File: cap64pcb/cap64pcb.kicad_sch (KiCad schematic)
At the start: 31 parts, among them J1 SM05B_SURS_TF, Q1 BSS138, Q2 BSS138, U1 MPR121QR2, U2 SPX3819M5-L-3-3

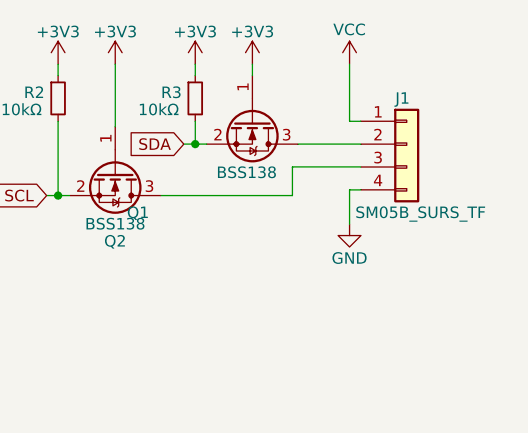
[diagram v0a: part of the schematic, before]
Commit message: reorder conn pinout
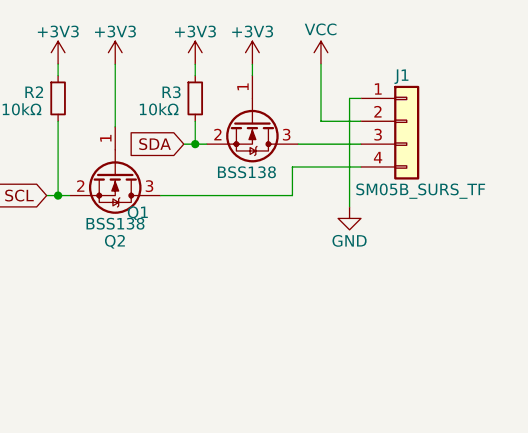
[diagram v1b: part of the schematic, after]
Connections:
- net GND: now also J1.1 (Pin_1); no longer J1.4 (Pin_4)
- net VCC: now also J1.2 (Pin_2); no longer J1.1 (Pin_1)
- net at Q1.3 (D): now also J1.3 (Pin_3); no longer J1.2 (Pin_2)
- net at Q2.3 (D): now also J1.4 (Pin_4); no longer J1.3 (Pin_3)
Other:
- moved on the sheet: J1
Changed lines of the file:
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@@
     (stroke (width 0) (type default) (color 0 0 0 0))
   )
-  (wire (pts (xy 179.07 40.005) (xy 179.07 46.355))
+  (wire (pts (xy 175.895 40.005) (xy 175.895 46.355))
     (stroke (width 0) (type default) (color 0 0 0 0))
   )
@@
     (stroke (width 0) (type default) (color 0 0 0 0))
   )
-  (wire (pts (xy 179.07 53.975) (xy 180.34 53.975))
-    (stroke (width 0) (type default) (color 0 0 0 0))
-  )
   (wire (pts (xy 58.42 50.165) (xy 58.42 52.705))
     (stroke (width 0) (type default) (color 0 0 0 0))
@@
     (stroke (width 0) (type default) (color 0 0 0 0))
   )
-  (wire (pts (xy 179.07 46.355) (xy 180.34 46.355))
+  (wire (pts (xy 175.895 46.355) (xy 180.34 46.355))
     (stroke (width 0) (type default) (color 0 0 0 0))
   )
@@
     (stroke (width 0) (type default) (color 0 0 0 0))
   )
+  (wire (pts (xy 179.07 43.815) (xy 179.07 55.88))
+    (stroke (width 0) (type default) (color 0 0 0 0))
+  )
   (wire (pts (xy 97.79 56.515) (xy 100.33 56.515))
     (stroke (width 0) (type default) (color 0 0 0 0))
@@
     (stroke (width 0) (type default) (color 0 0 0 0))
   )
+  (wire (pts (xy 180.34 43.815) (xy 179.07 43.815))
+    (stroke (width 0) (type default) (color 0 0 0 0))
+  )
   (wire (pts (xy 88.265 61.595) (xy 88.265 64.135))
     (stroke (width 0) (type default) (color 0 0 0 0))
@@
   )
   (wire (pts (xy 125.73 56.515) (xy 127 56.515))
-    (stroke (width 0) (type default) (color 0 0 0 0))
-  )
-  (wire (pts (xy 179.07 53.975) (xy 179.07 57.785))
     (stroke (width 0) (type default) (color 0 0 0 0))
   )
@@
     (pin "1")
   )
-  (symbol (lib_id "Connector_Generic:Conn_01x04") (at 185.42 48.895 0) (unit 1)
-    (in_bom yes) (on_board yes)
-    (property "Reference" "J1" (id 0) (at 184.15 43.815 0)
-      (effects (font (size 1.27 1.27)) (justify left))
-    )
-    (property "Value" "SM05B_SURS_TF" (id 1) (at 179.705 56.515 0)
-      (effects (font (size 1.27 1.27)) (justify left))
-    )
-    (property "Footprint" "Connector_JST:JST_SUR_SM04B-SURS-TF_1x04-1MP_P0.80mm_Horizontal" (id 2) (at 185.42 48.895 0)
-      (effects (font (size 1.27 1.27)) hide)
-    )
-    (property "Datasheet" "~" (id 3) (at 185.42 48.895 0)
+  (symbol (lib_id "Connector_Generic:Conn_01x04") (at 185.42 46.355 0) (unit 1)
+    (in_bom yes) (on_board yes)
+    (property "Reference" "J1" (id 0) (at 184.15 41.275 0)
+      (effects (font (size 1.27 1.27)) (justify left))
+    )
+    (property "Value" "SM05B_SURS_TF" (id 1) (at 179.705 53.975 0)
+      (effects (font (size 1.27 1.27)) (justify left))
+    )
+    (property "Footprint" "Connector_JST:JST_SUR_SM04B-SURS-TF_1x04-1MP_P0.80mm_Horizontal" (id 2) (at 185.42 46.355 0)
+      (effects (font (size 1.27 1.27)) hide)
+    )
+    (property "Datasheet" "~" (id 3) (at 185.42 46.355 0)
       (effects (font (size 1.27 1.27)) hide)
     )
@@
     (pin "1")
   )
-  (symbol (lib_id "power:GND") (at 179.07 57.785 0) (unit 1)
-    (in_bom yes) (on_board yes)
-    (property "Reference" "#PWR0114" (id 0) (at 179.07 64.135 0)
-      (effects (font (size 1.27 1.27)) hide)
-    )
-    (property "Value" "GND" (id 1) (at 179.07 61.595 0))
-    (property "Footprint" "" (id 2) (at 179.07 57.785 0)
-      (effects (font (size 1.27 1.27)) hide)
-    )
-    (property "Datasheet" "" (id 3) (at 179.07 57.785 0)
+  (symbol (lib_id "power:GND") (at 179.07 55.88 0) (unit 1)
+    (in_bom yes) (on_board yes)
+    (property "Reference" "#PWR0114" (id 0) (at 179.07 62.23 0)
+      (effects (font (size 1.27 1.27)) hide)
+    )
+    (property "Value" "GND" (id 1) (at 179.07 59.69 0))
+    (property "Footprint" "" (id 2) (at 179.07 55.88 0)
+      (effects (font (size 1.27 1.27)) hide)
+    )
+    (property "Datasheet" "" (id 3) (at 179.07 55.88 0)
       (effects (font (size 1.27 1.27)) hide)
     )
@@
     (pin "1")
   )
-  (symbol (lib_id "power:VCC") (at 179.07 40.005 0) (unit 1)
-    (in_bom yes) (on_board yes)
-    (property "Reference" "#PWR0117" (id 0) (at 179.07 43.815 0)
-      (effects (font (size 1.27 1.27)) hide)
-    )
-    (property "Value" "VCC" (id 1) (at 179.07 36.195 0))
-    (property "Footprint" "" (id 2) (at 179.07 40.005 0)
-      (effects (font (size 1.27 1.27)) hide)
-    )
-    (property "Datasheet" "" (id 3) (at 179.07 40.005 0)
-      (effects (font (size 1.27 1.27)) hide)
-    )
+  (symbol (lib_id "power:VCC") (at 175.895 40.005 0) (unit 1)
+    (in_bom yes) (on_board yes)
+    (property "Reference" "#PWR0117" (id 0) (at 175.895 43.815 0)
+      (effects (font (size 1.27 1.27)) hide)
+    )
+    (property "Value" "VCC" (id 1) (at 175.895 36.195 0))
+    (property "Footprint" "" (id 2) (at 175.895 40.005 0)
+      (effects (font (size 1.27 1.27)) hide)
+    )
+    (property "Datasheet" "" (id 3) (at 175.895 40.005 0)
+      (effects (font (size 1.27 1.27)) hide)
+    )

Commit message: tie MP to GND
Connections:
- net GND: now also J1.MP
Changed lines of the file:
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@@
     (stroke (width 0) (type default) (color 0 0 0 0))
   )
-  (wire (pts (xy 179.07 43.815) (xy 179.07 55.88))
+  (wire (pts (xy 179.07 43.815) (xy 179.07 56.515))
     (stroke (width 0) (type default) (color 0 0 0 0))
   )
@@
   )
   (wire (pts (xy 113.03 81.915) (xy 113.03 83.185))
+    (stroke (width 0) (type default) (color 0 0 0 0))
+  )
+  (wire (pts (xy 185.42 55.245) (xy 185.42 56.515))
     (stroke (width 0) (type default) (color 0 0 0 0))
   )
@@
       (effects (font (size 1.27 1.27)) (justify left))
     )
-    (property "Value" "SM05B_SURS_TF" (id 1) (at 179.705 53.975 0)
+    (property "Value" "SM05B_SURS_TF" (id 1) (at 188.595 54.61 90)
       (effects (font (size 1.27 1.27)) (justify left))
     )
@@
     (pin "3")
     (pin "4")
+    (pin "MP")
   )
   (symbol (lib_id "Regulator_Linear:SPX3819M5-L-3-3") (at 35.56 43.815 0) (unit 1)
@@
     )
     (property "Datasheet" "" (id 3) (at 78.105 83.185 0)
+      (effects (font (size 1.27 1.27)) hide)
+    )
+    (pin "1")
+  )
+  (symbol (lib_id "power:GND") (at 185.42 56.515 0) (unit 1)
+    (in_bom yes) (on_board yes)
+    (property "Reference" "#PWR?" (id 0) (at 185.42 62.865 0)
+      (effects (font (size 1.27 1.27)) hide)
+    )
+    (property "Value" "GND" (id 1) (at 185.42 60.325 0))
+    (property "Footprint" "" (id 2) (at 185.42 56.515 0)
+      (effects (font (size 1.27 1.27)) hide)
+    )
+    (property "Datasheet" "" (id 3) (at 185.42 56.515 0)
       (effects (font (size 1.27 1.27)) hide)
     )
@@
     (pin "1")
   )
-  (symbol (lib_id "power:GND") (at 179.07 55.88 0) (unit 1)
-    (in_bom yes) (on_board yes)
-    (property "Reference" "#PWR0114" (id 0) (at 179.07 62.23 0)
-      (effects (font (size 1.27 1.27)) hide)
-    )
-    (property "Value" "GND" (id 1) (at 179.07 59.69 0))
-    (property "Footprint" "" (id 2) (at 179.07 55.88 0)
-      (effects (font (size 1.27 1.27)) hide)
-    )
-    (property "Datasheet" "" (id 3) (at 179.07 55.88 0)
+  (symbol (lib_id "power:GND") (at 179.07 56.515 0) (unit 1)
+    (in_bom yes) (on_board yes)
+    (property "Reference" "#PWR0114" (id 0) (at 179.07 62.865 0)
+      (effects (font (size 1.27 1.27)) hide)
+    )
+    (property "Value" "GND" (id 1) (at 179.07 60.325 0))
+    (property "Footprint" "" (id 2) (at 179.07 56.515 0)
+      (effects (font (size 1.27 1.27)) hide)
+    )
+    (property "Datasheet" "" (id 3) (at 179.07 56.515 0)
       (effects (font (size 1.27 1.27)) hide)
     )
@@
       (reference "#PWR0120") (unit 1) (value "+3V3") (footprint "")
     )
+    (path "/4de64f1d-704e-4f11-85eb-52a828b3fd02"
+      (reference "#PWR?") (unit 1) (value "GND") (footprint "")
+    )
     (path "/f135c53c-386c-4051-aa9a-f8f2f6913b14"

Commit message: better routing
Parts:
- D1: value RED -> INT
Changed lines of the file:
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@@
   (symbol (lib_id "power:GND") (at 185.42 56.515 0) (unit 1)
     (in_bom yes) (on_board yes)
-    (property "Reference" "#PWR?" (id 0) (at 185.42 62.865 0)
+    (property "Reference" "#PWR0121" (id 0) (at 185.42 62.865 0)
       (effects (font (size 1.27 1.27)) hide)
     )
@@
       (effects (font (size 1.27 1.27)) (justify right))
     )
-    (property "Value" "RED" (id 1) (at 96.52 57.785 0)
+    (property "Value" "INT" (id 1) (at 96.52 57.785 0)
       (effects (font (size 1.27 1.27)) (justify right))
     )
@@
     )
     (path "/4de64f1d-704e-4f11-85eb-52a828b3fd02"
-      (reference "#PWR?") (unit 1) (value "GND") (footprint "")
+      (reference "#PWR0121") (unit 1) (value "GND") (footprint "")
     )
     (path "/f135c53c-386c-4051-aa9a-f8f2f6913b14"
@@
     )
     (path "/c99a01b3-5224-46b3-9237-a21f39c43bb5"
-      (reference "D1") (unit 1) (value "RED") (footprint "LED_SMD:LED_0805_2012Metric")
+      (reference "D1") (unit 1) (value "INT") (footprint "LED_SMD:LED_0805_2012Metric")
     )
     (path "/19d8f5e6-7917-4311-ae54-a6b4c084a96c"

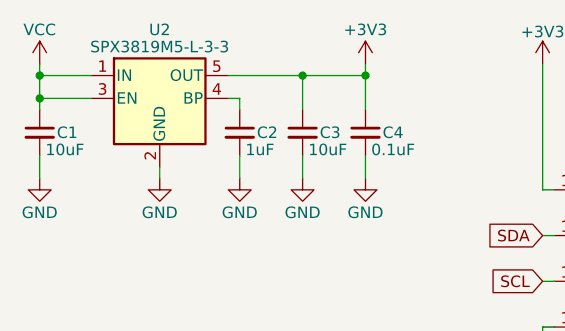
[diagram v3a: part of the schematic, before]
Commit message: logo and up to ADDR jumpers
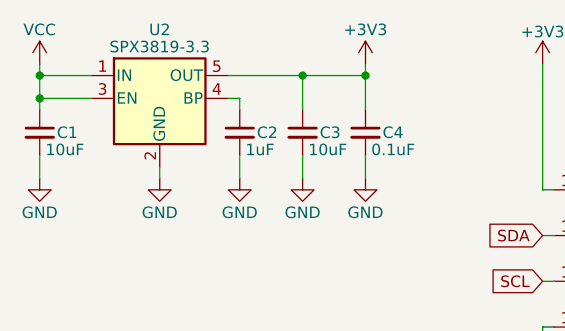
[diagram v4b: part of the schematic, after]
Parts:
- JP1: value 3V3 -> B
- JP2: value SDA -> C
- JP3: value SCL -> D
- JP4: value GND -> A
- U2: value SPX3819M5-L-3-3 -> SPX3819-3.3
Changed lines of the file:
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@@
     (in_bom yes) (on_board yes)
     (property "Reference" "JP3" (id 0) (at 83.185 62.23 0))
-    (property "Value" "SCL" (id 1) (at 83.185 62.0831 0)
+    (property "Value" "D" (id 1) (at 83.185 62.0831 0)
       (effects (font (size 1.27 1.27)) hide)
     )
@@
     (in_bom yes) (on_board yes)
     (property "Reference" "U2" (id 0) (at 35.56 36.195 0))
-    (property "Value" "SPX3819M5-L-3-3" (id 1) (at 35.56 38.1 0))
+    (property "Value" "SPX3819-3.3" (id 1) (at 35.56 38.1 0))
     (property "Footprint" "Package_TO_SOT_SMD:SOT-23-5" (id 2) (at 35.56 35.56 0)
       (effects (font (size 1.27 1.27)) hide)
@@
     (in_bom yes) (on_board yes)
     (property "Reference" "JP2" (id 0) (at 83.185 57.15 0))
-    (property "Value" "SDA" (id 1) (at 83.185 57.0031 0)
+    (property "Value" "C" (id 1) (at 83.185 57.0031 0)
       (effects (font (size 1.27 1.27)) hide)
     )
@@
     (in_bom yes) (on_board yes)
     (property "Reference" "JP1" (id 0) (at 83.185 52.07 0))
-    (property "Value" "3V3" (id 1) (at 83.185 51.9231 0)
+    (property "Value" "B" (id 1) (at 83.185 51.9231 0)
       (effects (font (size 1.27 1.27)) hide)
     )
@@
     (in_bom yes) (on_board yes)
     (property "Reference" "JP4" (id 0) (at 83.185 67.31 0))
-    (property "Value" "GND" (id 1) (at 83.185 67.1631 0)
+    (property "Value" "A" (id 1) (at 83.185 67.1631 0)
       (effects (font (size 1.27 1.27)) hide)
     )
@@
     )
     (path "/b34742e1-ce68-4d8f-ad70-c480e9f9e995"
-      (reference "JP1") (unit 1) (value "3V3") (footprint "Jumper:SolderJumper-2_P1.3mm_Open_RoundedPad1.0x1.5mm")
+      (reference "JP1") (unit 1) (value "B") (footprint "Jumper:SolderJumper-2_P1.3mm_Open_RoundedPad1.0x1.5mm")
     )
     (path "/7b357652-d43b-4655-9b9a-32e855a5ce28"
-      (reference "JP2") (unit 1) (value "SDA") (footprint "Jumper:SolderJumper-2_P1.3mm_Open_RoundedPad1.0x1.5mm")
+      (reference "JP2") (unit 1) (value "C") (footprint "Jumper:SolderJumper-2_P1.3mm_Open_RoundedPad1.0x1.5mm")
     )
     (path "/026c75c1-77c0-4d35-bec2-ff672e1eb123"
-      (reference "JP3") (unit 1) (value "SCL") (footprint "Jumper:SolderJumper-2_P1.3mm_Open_RoundedPad1.0x1.5mm")
+      (reference "JP3") (unit 1) (value "D") (footprint "Jumper:SolderJumper-2_P1.3mm_Open_RoundedPad1.0x1.5mm")
     )
     (path "/e64971c2-dc20-4371-a7b6-efa95ea9404e"
-      (reference "JP4") (unit 1) (value "GND") (footprint "Jumper:SolderJumper-2_P1.3mm_Bridged_RoundedPad1.0x1.5mm")
+      (reference "JP4") (unit 1) (value "A") (footprint "Jumper:SolderJumper-2_P1.3mm_Bridged_RoundedPad1.0x1.5mm")
     )
     (path "/4df03174-9603-43d2-88cc-bd6346b3f204"
@@
     )
     (path "/1ba2f91d-40ab-4f54-827b-9c0abde8d7d9"
-      (reference "U2") (unit 1) (value "SPX3819M5-L-3-3") (footprint "Package_TO_SOT_SMD:SOT-23-5")
-    )
-  )
+      (reference "U2") (unit 1) (value "SPX3819-3.3") (footprint "Package_TO_SOT_SMD:SOT-23-5")
+    )
+  )

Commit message: pretty!
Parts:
- removed JP1: B, Jumper:SolderJumper-2_P1.3mm_Open_RoundedPad1.0x1.5mm, symbol Jumper:SolderJumper_2_Open
- removed JP2: C, Jumper:SolderJumper-2_P1.3mm_Open_RoundedPad1.0x1.5mm, symbol Jumper:SolderJumper_2_Open
- removed JP3: D, Jumper:SolderJumper-2_P1.3mm_Open_RoundedPad1.0x1.5mm, symbol Jumper:SolderJumper_2_Open
- removed JP4: A, Jumper:SolderJumper-2_P1.3mm_Bridged_RoundedPad1.0x1.5mm, symbol Jumper:SolderJumper_2_Bridged
- added JP1: SolderJumper_3_Open, Jumper:SolderJumper-3_P1.3mm_Open_RoundedPad1.0x1.5mm_NumberLabels, symbol Jumper:SolderJumper_3_Open
- added TP13: b, TestPoint:TestPoint_Pad_2.0x2.0mm, symbol Connector:TestPoint
- added TP14: d, TestPoint:TestPoint_Pad_2.0x2.0mm, symbol Connector:TestPoint
- J1: value SM05B_SURS_TF -> SM04B_SURS_TF
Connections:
- net +3V3: now also TP13.1
- net GND: now also JP1.1 (A)
- net SCL: now also TP14.1
- net SDA: now also JP1.3 (B)
- net at U1.4 (ADDR): now also JP1.2 (C)
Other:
- moved on the sheet: R4
